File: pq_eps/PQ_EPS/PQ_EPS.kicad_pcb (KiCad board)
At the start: 2 copper layers, 40 x 40 mm, 77 parts, among them IC2 ISL9120IRTNZ, J1 SLW-110-01-X-S, J2 SLW-110-01-X-S, J3 SLW-110-01-X-S, J4 SLW-110-01-X-S, Q1 SIR424DP-T1-GE3

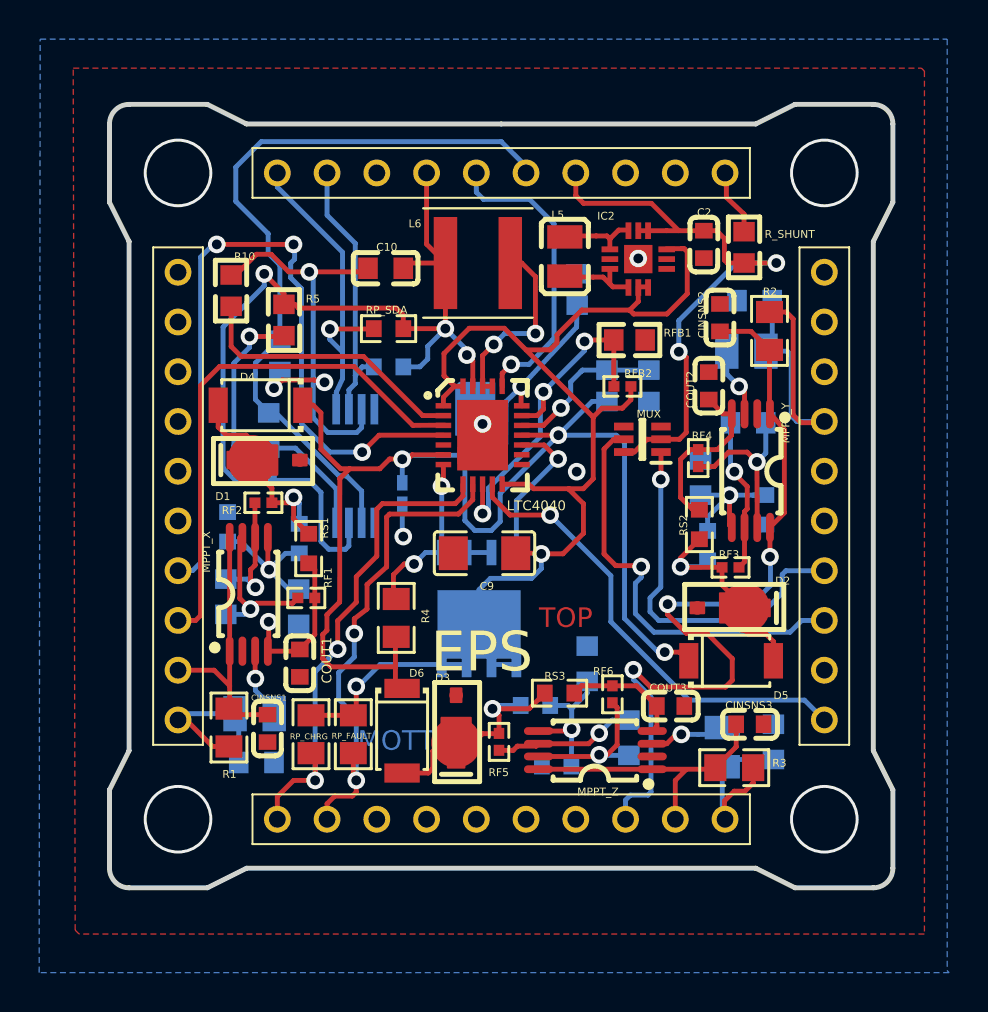
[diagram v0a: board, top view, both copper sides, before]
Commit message: eps port to kicad corrected
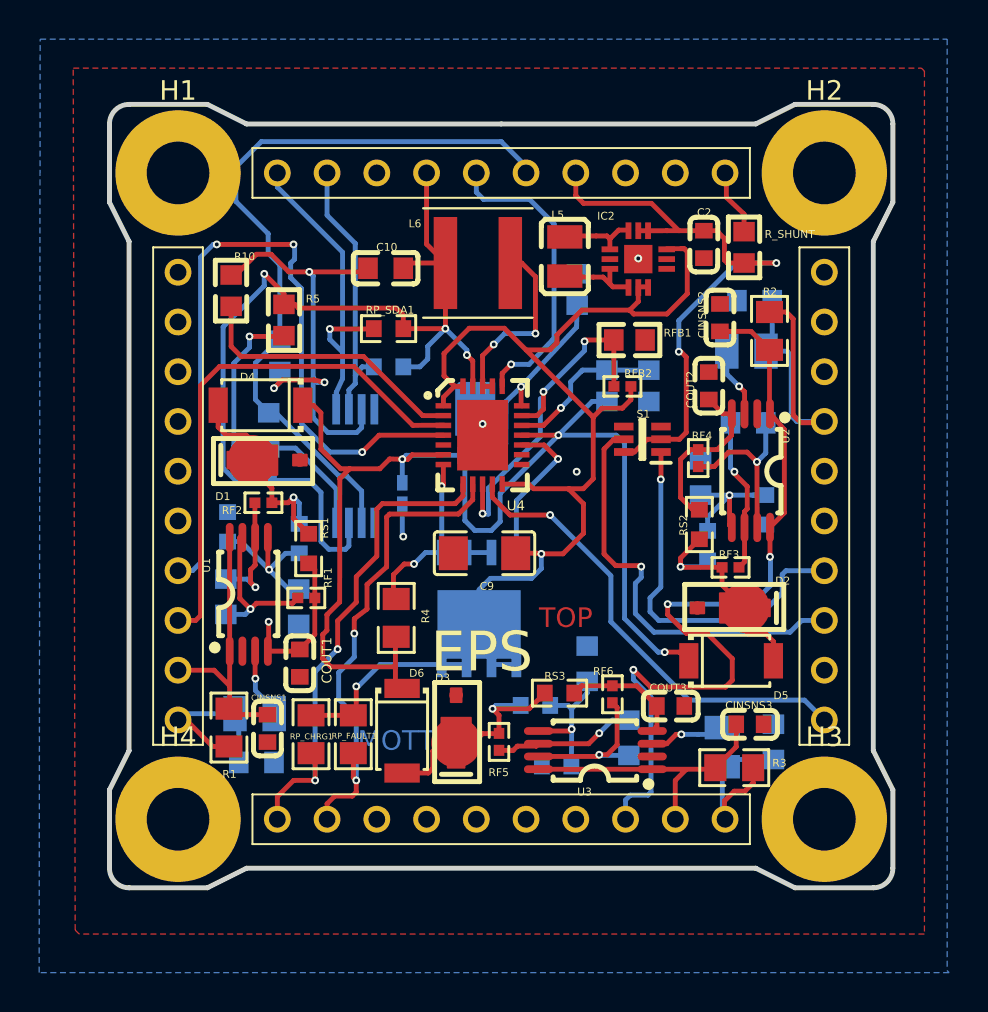
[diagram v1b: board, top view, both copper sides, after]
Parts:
- added H1: MountingHole_Pad, MountingHole:MountingHole_3.2mm_M3_Pad, F.Cu at (85.2, 41.5)
- added H2: MountingHole_Pad, MountingHole:MountingHole_3.2mm_M3_Pad, F.Cu at (118.2, 41.5)
- added H3: MountingHole_Pad, MountingHole:MountingHole_3.2mm_M3_Pad, F.Cu at (118.2, 74.5)
- added H4: MountingHole_Pad, MountingHole:MountingHole_3.2mm_M3_Pad, F.Cu at (85.2, 74.5)
- CINSNS1, CINSNS2, CINSNS3: value 10u -> 1n
- D4, D5, D6: value PDZVTR4.7B -> shottky
- J1, J2, J3, J4: value SLW-110-01-X-S -> SLW-110-01-T-S
- RFB1: value 100m -> 68k
- renumbered DS2782E+ to IC1, RP_CHRG to RP_CHRG1, RP_FAULT to RP_FAULT1, RP_SCL to RP_SCL1, RP_SDA to RP_SDA1, MUX to S1, MPPT_X to U1, MPPT_Y to U2, MPPT_Z to U3, LTC4040 to U4
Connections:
- C1 pad 1: (no net) -> Net-(C1-Pad1)
- C1 pad 2: (no net) -> /BATT-
- C10 pad 1: (no net) -> /BATT+
- C10 pad 2: (no net) -> GND
- C2 pad 1: (no net) -> GND
- C2 pad 2: (no net) -> /VCC
- C8 pad 1: (no net) -> /OVSNS
- C8 pad 2: (no net) -> GND
- C9 pad 1: (no net) -> /CHOUT
- C9 pad 2: (no net) -> GND
- CF1 pad 1: (no net) -> Net-(CF1-Pad1)
- CF1 pad 2: (no net) -> Net-(CF1-Pad2)
- CF2 pad 1: (no net) -> Net-(CF2-Pad1)
- CF2 pad 2: (no net) -> Net-(CF2-Pad2)
- CF3 pad 1: (no net) -> Net-(CF3-Pad1)
- CF3 pad 2: (no net) -> Net-(CF3-Pad2)
- CIN1 pad 1: (no net) -> GND
- CIN1 pad 2: (no net) -> /SOLAR_X
- CIN2 pad 1: (no net) -> GND
- CIN2 pad 2: (no net) -> /SOLAR_Y
- CIN3 pad 1: (no net) -> GND
- CIN3 pad 2: (no net) -> /SOLAR_Z
- CINSNS1 pad 1: (no net) -> GND
- CINSNS1 pad 2: (no net) -> /MPPT_X
- CINSNS2 pad 1: (no net) -> GND
- CINSNS2 pad 2: (no net) -> /MPPT_Y
- CINSNS3 pad 1: (no net) -> GND
- CINSNS3 pad 2: (no net) -> /MPPT_Z
- COUT1 pad 1: (no net) -> GND
- COUT1 pad 2: (no net) -> Net-(COUT1-Pad2)
- COUT2 pad 1: (no net) -> GND
- COUT2 pad 2: (no net) -> Net-(COUT2-Pad2)
- COUT3 pad 1: (no net) -> GND
- COUT3 pad 2: (no net) -> Net-(COUT3-Pad2)
- COUTSNS1 pad 1: (no net) -> GND
- COUTSNS1 pad 2: (no net) -> Net-(COUTSNS1-Pad2)
- COUTSNS2 pad 1: (no net) -> GND
- COUTSNS2 pad 2: (no net) -> Net-(COUTSNS2-Pad2)
- COUTSNS3 pad 1: (no net) -> GND
- COUTSNS3 pad 2: (no net) -> Net-(COUTSNS3-Pad2)
- D1 pad 1: (no net) -> GND
- D1 pad 2: (no net) -> Net-(D1-Pad2)
- D2 pad 1: (no net) -> GND
- D2 pad 2: (no net) -> Net-(D2-Pad2)
- D3 pad 1: (no net) -> GND
- D3 pad 2: (no net) -> Net-(D3-Pad2)
- D4 pad 1: (no net) -> /OVSNS
- D4 pad 2: (no net) -> Net-(D1-Pad2)
- D5 pad 1: (no net) -> /OVSNS
- D5 pad 2: (no net) -> Net-(D2-Pad2)
- D6 pad 1: (no net) -> /OVSNS
- D6 pad 2: (no net) -> Net-(D3-Pad2)
- IC1 pad 1: (no net) -> unconnected-(IC1-Pad1)
- IC1 pad 2: (no net) -> /BATT-
- IC1 pad 3: (no net) -> Net-(IC1-Pad3)
- IC1 pad 4: (no net) -> Net-(C1-Pad1)
- IC1 pad 5: (no net) -> /SCL
- IC1 pad 6: (no net) -> /SCL
- IC1 pad 7: (no net) -> GND
- IC1 pad 8: (no net) -> unconnected-(IC1-Pad8)
- IC2 pad 1: (no net) -> Net-(L5-Pad2)
- IC2 pad 10: (no net) -> /VCC
- IC2 pad 11: (no net) -> /VCC
- IC2 pad 12: (no net) -> Net-(L5-Pad2)
- IC2 pad 13: (no net) -> GND
- IC2 pad 2: (no net) -> GND
- IC2 pad 3: (no net) -> Net-(L5-Pad1)
- IC2 pad 4: (no net) -> Net-(L5-Pad1)
- IC2 pad 5: (no net) -> /CHOUT
- IC2 pad 6: (no net) -> /CHOUT
- IC2 pad 7: (no net) -> GND
- IC2 pad 8: (no net) -> GND
- IC2 pad 9: (no net) -> /CHOUT
- J1 pad 1: (no net) -> /SCL
- J1 pad 10: (no net) -> /VCC
- J1 pad 2: (no net) -> /SCL
- J1 pad 3: (no net) -> unconnected-(J1-Pad3)
- J1 pad 4: (no net) -> /BATT+
- J1 pad 5: (no net) -> /PFO
- J1 pad 6: (no net) -> /BATT-
- J1 pad 7: (no net) -> unconnected-(J1-Pad7)
- J1 pad 8: (no net) -> unconnected-(J1-Pad8)
- J1 pad 9: (no net) -> GND
- J2 pad 1: (no net) -> unconnected-(J2-Pad1)
- J2 pad 10: (no net) -> /RST
- J2 pad 2: (no net) -> unconnected-(J2-Pad2)
- J2 pad 3: (no net) -> unconnected-(J2-Pad3)
- J2 pad 4: (no net) -> /SOLAR_Y
- J2 pad 5: (no net) -> unconnected-(J2-Pad5)
- J2 pad 6: (no net) -> unconnected-(J2-Pad6)
- J2 pad 7: (no net) -> /SEL
- J2 pad 8: (no net) -> /HEATER
- J2 pad 9: (no net) -> unconnected-(J2-Pad9)
- J3 pad 1: (no net) -> /CHRG
- J3 pad 10: (no net) -> /SOLAR_Z
- J3 pad 2: (no net) -> /FAULT
- J3 pad 3: (no net) -> unconnected-(J3-Pad3)
- J3 pad 4: (no net) -> unconnected-(J3-Pad4)
- J3 pad 5: (no net) -> unconnected-(J3-Pad5)
- J3 pad 6: (no net) -> unconnected-(J3-Pad6)
- J3 pad 7: (no net) -> unconnected-(J3-Pad7)
- J3 pad 8: (no net) -> /MPPT_Y
- J3 pad 9: (no net) -> /MPPT_Z
- J4 pad 1: (no net) -> unconnected-(J4-Pad1)
- J4 pad 10: (no net) -> /SOLAR_X
- J4 pad 2: (no net) -> unconnected-(J4-Pad2)
- J4 pad 3: (no net) -> unconnected-(J4-Pad3)
- J4 pad 4: (no net) -> unconnected-(J4-Pad4)
- J4 pad 5: (no net) -> unconnected-(J4-Pad5)
- J4 pad 6: (no net) -> unconnected-(J4-Pad6)
- J4 pad 7: (no net) -> /CHGOFF
- J4 pad 8: (no net) -> /CLPROG
- J4 pad 9: (no net) -> /MPPT_X
- L1 pad 1: (no net) -> /SOLAR_X
- L1 pad 2: (no net) -> Net-(U1-Pad3)
- L2 pad 1: (no net) -> /SOLAR_Y
- L2 pad 2: (no net) -> Net-(L2-Pad2)
- L3 pad 1: (no net) -> /SOLAR_Z
- L3 pad 2: (no net) -> Net-(U3-Pad3)
- L5 pad 1: (no net) -> Net-(L5-Pad1)
- L5 pad 2: (no net) -> Net-(L5-Pad2)
- L6 pad 1: (no net) -> /BATT+
- L6 pad 2: (no net) -> Net-(U4-Pad21)
- Q1 pad 1: (no net) -> Net-(Q1-Pad1)
- Q1 pad 2: (no net) -> Net-(Q1-Pad1)
- Q1 pad 3: (no net) -> Net-(Q1-Pad1)
- Q1 pad 4: (no net) -> Net-(Q1-Pad4)
- Q1 pad 5: (no net) -> /CHOUT
- Q1 pad 6: (no net) -> /CHOUT
- Q1 pad 7: (no net) -> /CHOUT
- Q1 pad 8: (no net) -> /CHOUT
- R1 pad 1: (no net) -> /SOLAR_X
- R1 pad 2: (no net) -> /MPPT_X
- R10 pad 1: (no net) -> /PROG
- R10 pad 2: (no net) -> GND
- R2 pad 1: (no net) -> /SOLAR_Y
- R2 pad 2: (no net) -> /MPPT_Y
- R3 pad 1: (no net) -> /SOLAR_Z
- R3 pad 2: (no net) -> /MPPT_Z
- R4 pad 1: (no net) -> Net-(Q1-Pad1)
- R4 pad 2: (no net) -> /OVSNS
- R5 pad 1: (no net) -> /BATT+
- R5 pad 2: (no net) -> Net-(C1-Pad1)
- R6 pad 1: (no net) -> GND
- R6 pad 2: (no net) -> /BATT-
- R7 pad 1: (no net) -> /BATT+
- R7 pad 2: (no net) -> Net-(IC1-Pad3)
- R8 pad 1: (no net) -> GND
- R8 pad 2: (no net) -> /NTC
- R9 pad 1: (no net) -> /NTC
- R9 pad 2: (no net) -> /OVSNS
- RF1 pad 1: (no net) -> Net-(CF1-Pad2)
- RF1 pad 2: (no net) -> Net-(COUT1-Pad2)
- RF2 pad 1: (no net) -> Net-(CF1-Pad1)
- RF2 pad 2: (no net) -> Net-(D1-Pad2)
- RF3 pad 1: (no net) -> Net-(CF2-Pad1)
- RF3 pad 2: (no net) -> Net-(D2-Pad2)
- RF4 pad 1: (no net) -> Net-(CF2-Pad2)
- RF4 pad 2: (no net) -> Net-(COUT2-Pad2)
- RF5 pad 1: (no net) -> Net-(CF3-Pad1)
- RF5 pad 2: (no net) -> Net-(D3-Pad2)
- RF6 pad 1: (no net) -> Net-(CF3-Pad2)
- RF6 pad 2: (no net) -> Net-(COUT3-Pad2)
- RFB1 pad 1: (no net) -> Net-(RFB1-Pad1)
- RFB1 pad 2: (no net) -> GND
- RFB2 pad 1: (no net) -> Net-(RFB1-Pad1)
- RFB2 pad 2: (no net) -> /CHOUT
- RH1 pad 1: (no net) -> Net-(COUTSNS1-Pad2)
- RH1 pad 2: (no net) -> Net-(D1-Pad2)
- RH2 pad 1: (no net) -> Net-(COUTSNS2-Pad2)
- RH2 pad 2: (no net) -> Net-(D2-Pad2)
- RH3 pad 1: (no net) -> Net-(COUTSNS3-Pad2)
- RH3 pad 2: (no net) -> Net-(D3-Pad2)
- RL1 pad 1: (no net) -> GND
- RL1 pad 2: (no net) -> Net-(COUTSNS1-Pad2)
- RL2 pad 1: (no net) -> GND
- RL2 pad 2: (no net) -> Net-(COUTSNS2-Pad2)
- RL3 pad 1: (no net) -> GND
- RL3 pad 2: (no net) -> Net-(COUTSNS3-Pad2)
- RPF1 pad 1: (no net) -> /OVSNS
- RPF1 pad 2: (no net) -> Net-(RPF1-Pad2)
- RPF2 pad 1: (no net) -> Net-(RPF1-Pad2)
- RPF2 pad 2: (no net) -> GND
- RP_CHRG1 pad 1: (no net) -> /CHRG
- RP_CHRG1 pad 2: (no net) -> /CHOUT
- RP_FAULT1 pad 1: (no net) -> /FAULT
- RP_FAULT1 pad 2: (no net) -> /CHOUT
- RP_SCL1 pad 1: (no net) -> /BATT+
- RP_SCL1 pad 2: (no net) -> /SCL
- RP_SDA1 pad 1: (no net) -> /BATT+
- RP_SDA1 pad 2: (no net) -> /SCL
- RS1 pad 1: (no net) -> Net-(COUT1-Pad2)
- RS1 pad 2: (no net) -> Net-(D1-Pad2)
- RS2 pad 1: (no net) -> Net-(COUT2-Pad2)
- RS2 pad 2: (no net) -> Net-(D2-Pad2)
- RS3 pad 1: (no net) -> Net-(COUT3-Pad2)
- RS3 pad 2: (no net) -> Net-(D3-Pad2)
- S1 pad 1: (no net) -> /SEL
- S1 pad 2: (no net) -> /TOTAL_CURRENT
- S1 pad 3: (no net) -> GND
- S1 pad 4: (no net) -> GND
- S1 pad 5: (no net) -> /HEATER
- S1 pad 6: (no net) -> /TOTAL_CURRENT
- U1 pad 1: (no net) -> /MPPT_X
- U1 pad 2: (no net) -> GND
- U1 pad 3: (no net) -> Net-(U1-Pad3)
- U1 pad 4: (no net) -> Net-(COUT1-Pad2)
- U1 pad 5: (no net) -> Net-(COUTSNS1-Pad2)
- U1 pad 6: (no net) -> Net-(CF1-Pad1)
- U1 pad 7: (no net) -> Net-(CF1-Pad2)
- U1 pad 8: (no net) -> /MPPT_X
- U2 pad 1: (no net) -> /MPPT_Y
- U2 pad 2: (no net) -> GND
- U2 pad 3: (no net) -> Net-(L2-Pad2)
- U2 pad 4: (no net) -> Net-(COUT2-Pad2)
- U2 pad 5: (no net) -> Net-(COUTSNS2-Pad2)
- U2 pad 6: (no net) -> Net-(CF2-Pad1)
- U2 pad 7: (no net) -> Net-(CF2-Pad2)
- U2 pad 8: (no net) -> /MPPT_Y
- U3 pad 1: (no net) -> /MPPT_Z
- U3 pad 2: (no net) -> GND
- U3 pad 3: (no net) -> Net-(U3-Pad3)
- U3 pad 4: (no net) -> Net-(COUT3-Pad2)
- U3 pad 5: (no net) -> Net-(COUTSNS3-Pad2)
- U3 pad 6: (no net) -> Net-(CF3-Pad1)
- U3 pad 7: (no net) -> Net-(CF3-Pad2)
- U3 pad 8: (no net) -> /MPPT_Z
- U4 pad 1: (no net) -> /CHOUT
- U4 pad 10: (no net) -> Net-(RFB1-Pad1)
- U4 pad 11: (no net) -> /RST
- U4 pad 12: (no net) -> /CHOUT
- U4 pad 13: (no net) -> GND
- U4 pad 14: (no net) -> GND
- U4 pad 15: (no net) -> Net-(Q1-Pad4)
- U4 pad 16: (no net) -> /OVSNS
- U4 pad 17: (no net) -> /NTC
- U4 pad 18: (no net) -> Net-(RFB1-Pad1)
- U4 pad 19: (no net) -> Net-(RPF1-Pad2)
- U4 pad 2: (no net) -> /PROG
- U4 pad 20: (no net) -> /PFO
- U4 pad 21: (no net) -> Net-(U4-Pad21)
- U4 pad 22: (no net) -> Net-(U4-Pad21)
- U4 pad 23: (no net) -> /BATT+
- U4 pad 24: (no net) -> /CHOUT
- U4 pad 25: (no net) -> GND
- U4 pad 3: (no net) -> /CLPROG
- U4 pad 4: (no net) -> /CHGOFF
- U4 pad 5: (no net) -> GND
- U4 pad 6: (no net) -> /OVSNS
- U4 pad 7: (no net) -> Net-(Q1-Pad1)
- U4 pad 8: (no net) -> /CHRG
- U4 pad 9: (no net) -> /FAULT
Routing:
- net (no net): track 854.4 -> 0.00 mm, vias 63 -> 0
- net /OVSNS: track 0.00 -> 64.3 mm, vias 0 -> 3
- net /CHOUT: track 0.00 -> 63.8 mm, vias 0 -> 2
- net /MPPT_Y: track 0.00 -> 41.7 mm, vias 0 -> 3
- net /BATT+: track 0.00 -> 41.4 mm, vias 0 -> 3
- net /CHGOFF: track 0.00 -> 39.6 mm, vias 0 -> 3
- net /BATT-: track 0.00 -> 38.6 mm
- net /VCC: track 0.00 -> 34.7 mm, vias 0 -> 2
- net /SCL: track 0.00 -> 31.2 mm, vias 0 -> 1
- net /CLPROG: track 0.00 -> 27.1 mm
- net /CHRG: track 0.00 -> 25.3 mm, vias 0 -> 2
- net GND: track 0.00 -> 25.3 mm, vias 0 -> 7
- net /FAULT: track 0.00 -> 25.1 mm, vias 0 -> 2
- net /RST: track 0.00 -> 23.7 mm, vias 0 -> 1
- net /HEATER: track 0.00 -> 21.5 mm, vias 0 -> 1
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- added copper zone on B.Cu, net GND
- added copper zone on F.Cu, net GND
- removed copper zone on B.Cu, net (none)
- removed copper zone on F.Cu, net (none)

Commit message: EPS LTC 4040 correction and layout revamp
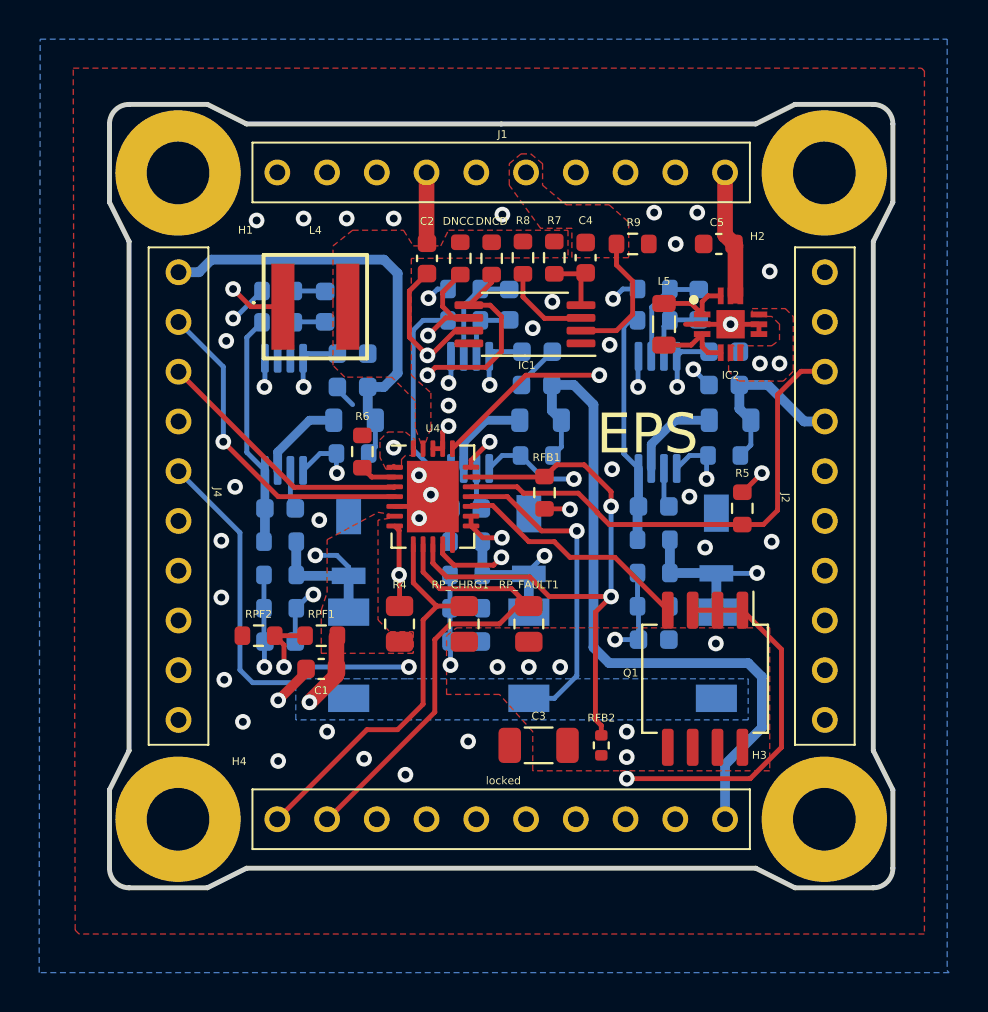
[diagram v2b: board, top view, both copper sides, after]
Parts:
- removed C10: 10u, easyeda:C0603
- removed C8: 2.2u, easyeda:C0402
- removed C9: 100u, easyeda:C1206
- removed L6: 2.2u, easyeda:L_COILCRAFT_XAL5030
- removed R10: 14k, easyeda:R0603
- removed RP_SCL1, RP_SDA1: 20k, easyeda:R0603
- removed R_SHUNT: 100m, easyeda:R0603
- removed S1: MUX, easyeda:SOT65P210X110-6N
- added C3: 100u, Capacitor_SMD:C_1206_3216Metric, F.Cu at (103.6, 70.7)
- added C4: 0.1u, Capacitor_SMD:C_0603_1608Metric, F.Cu at (106.0, 45.8)
- added C5: 22u, Capacitor_SMD:C_0603_1608Metric, F.Cu at (112.8, 45.1)
- added DNCC: 20k, Resistor_SMD:R_0603_1608Metric, F.Cu at (99.6, 45.8)
- added DNCD: 20k, Resistor_SMD:R_0603_1608Metric, F.Cu at (101.2, 45.8)
- added L4: XAL5030-222MEC, SamacSys_Parts:XAL5030222MEC, F.Cu at (92.2, 48.3)
- C1: value 0.1u -> 2.2u; footprint easyeda:C0603 -> Capacitor_SMD:C_0603_1608Metric
- C2: value 22u -> 10u; footprint easyeda:C0603 -> Capacitor_SMD:C_0603_1608Metric
- CF1, CF2, CF3, CIN1, CIN2, CIN3, CINSNS1, CINSNS2, CINSNS3, COUT1, COUT2, COUT3, COUTSNS1, COUTSNS2, COUTSNS3: footprint easyeda:C0603 -> Capacitor_SMD:C_0603_1608Metric; moved to B.Cu
- D1, D2, D3: footprint easyeda:DIO_SMM4F5.0A-TR -> SamacSys_Parts:SMM4F15ATR; moved to B.Cu
- D4, D5, D6: footprint easyeda:SOD-128_L3.7-W2.5-LS4.7-FD -> Diode_SMD:D_SOD-128; moved to B.Cu
- IC1: footprint easyeda:SOP65P640X110-8N -> Package_SO:TSSOP-8_4.4x3mm_P0.65mm
- IC2: footprint easyeda:QFN50P300X300X75-13N -> SamacSys_Parts:QFN50P300X300X75-13N-D
- J1, J2, J4: footprint easyeda:SLW-110-01-X-S -> NSL_Connectors:SLW-110-01-X-S
- L1, L2, L3: footprint easyeda:L0806 -> Inductor_SMD:L_0805_2012Metric; moved to B.Cu
- L5: footprint easyeda:L0806 -> Inductor_SMD:L_0805_2012Metric
- Q1: footprint easyeda:POWERPAK-SO-8_L6.2-W5.2-P1.27-BL-EP -> Package_SO:SO-8_5.3x6.2mm_P1.27mm
- R1, R2, R3: footprint easyeda:R0805 -> Resistor_SMD:R_0603_1608Metric; moved to B.Cu
- R4, RP_CHRG1, RP_FAULT1: footprint easyeda:R0805 -> Resistor_SMD:R_0805_2012Metric
- R5: value 510 -> 10k; footprint easyeda:R0603 -> Resistor_SMD:R_0603_1608Metric
- R6: value 15m -> 2k; footprint easyeda:R0603 -> Resistor_SMD:R_0603_1608Metric
- R7: value 1k -> 510; footprint easyeda:R0402 -> Resistor_SMD:R_0603_1608Metric
- R8: value 10k -> 1k; footprint easyeda:R0603 -> Resistor_SMD:R_0603_1608Metric
- R9: value 10k -> 15m; footprint easyeda:R0603 -> Resistor_SMD:R_0603_1608Metric
- RF1, RF2, RF3, RF4, RF5, RF6: footprint easyeda:R0402 -> Resistor_SMD:R_0603_1608Metric; moved to B.Cu
- RFB1, RPF1, RPF2: footprint easyeda:R0603 -> Resistor_SMD:R_0603_1608Metric
- RFB2: footprint easyeda:R0402 -> Resistor_SMD:R_0402_1005Metric
- RH1, RH2, RH3, RL1, RL2, RL3, RS1, RS2, RS3: footprint easyeda:R0603 -> Resistor_SMD:R_0603_1608Metric; moved to B.Cu
- U1, U2, U3: footprint easyeda:TSSOP-8_L4.4-W3.0-P0.65-LS6.4-BL -> Package_SO:TSSOP-8_4.4x3mm_P0.65mm; moved to B.Cu
- U4: footprint easyeda:VQFN-24_L5.0-W4.0-P0.50-BL-EP -> Package_DFN_QFN:QFN-24-1EP_4x5mm_P0.5mm_EP2.65x3.65mm
- locked: renamed from J3; footprint easyeda:SLW-110-01-X-S -> NSL_Connectors:SLW-110-01-X-S
- moved R5 25.3 mm to (114.0, 58.6), turned to 90 degrees
- moved RPF2 24.0 mm to (89.3, 65.1), turned to 180 degrees
- moved RF5 23.2 mm to (99.8, 47.4), turned to 180 degrees
- moved CF3 22.9 mm to (102.1, 48.2)
- moved CINSNS3 21.9 mm to (103.5, 50.6)
- moved CIN3 21.9 mm to (103.5, 52.3), turned to 0 degrees
- moved RF6 20.5 mm to (99.8, 49.0), turned to 180 degrees
- moved CIN1 19.8 mm to (94.1, 52.4)
- moved CINSNS1 19.6 mm to (94.1, 50.7), turned to 180 degrees
- moved L3 19.1 mm to (103.7, 54.1), turned to 180 degrees
- moved R3 18.9 mm to (103.5, 55.9)
- moved R7 18.7 mm to (104.4, 45.8), turned to -90 degrees
- moved U3 18.4 mm to (100.1, 53.7)
- moved RFB2 18.4 mm to (106.8, 70.7), turned to -90 degrees
- moved L1 15.8 mm to (94.2, 54.1), turned to 0 degrees
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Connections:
- C1 pad 1: Net-(C1-Pad1) -> /OVSNS
- C1 pad 2: /BATT- -> GND
- C2 pad 1: GND -> /KILLSWITCH+
- C2 pad 2: /VCC -> GND
- CINSNS1 pad 2: /MPPT_X -> Net-(CINSNS1-Pad2)
- CINSNS2 pad 2: /MPPT_Y -> Net-(CINSNS2-Pad2)
- CINSNS3 pad 2: /MPPT_Z -> Net-(CINSNS3-Pad2)
- IC1 pad 4: Net-(C1-Pad1) -> Net-(C4-Pad1)
- IC1 pad 5: /SCL -> /SDA
- J1 pad 1: /SCL -> /SDA
- J1 pad 4: /BATT+ -> /KILLSWITCH+
- J2 pad 10: /RST -> GND
- J2 pad 3: unconnected-(J2-Pad3) -> /BATT_NTC
- J2 pad 7: /SEL -> GND
- J2 pad 8: /HEATER -> unconnected-(J2-Pad8)
- J4 pad 1: unconnected-(J4-Pad1) -> /SOLAR_X
- J4 pad 10: /SOLAR_X -> unconnected-(J4-Pad10)
- J4 pad 2: unconnected-(J4-Pad2) -> /CHGOFF
- J4 pad 3: unconnected-(J4-Pad3) -> /CLPROG
- J4 pad 5: unconnected-(J4-Pad5) -> /RST
- J4 pad 7: /CHGOFF -> unconnected-(J4-Pad7)
- J4 pad 8: /CLPROG -> unconnected-(J4-Pad8)
- J4 pad 9: /MPPT_X -> unconnected-(J4-Pad9)
- L1 pad 1: /SOLAR_X -> Net-(L1-Pad1)
- L1 pad 2: Net-(U1-Pad3) -> /SOLAR_X
- R1 pad 2: /MPPT_X -> Net-(CINSNS1-Pad2)
- R2 pad 2: /MPPT_Y -> Net-(CINSNS2-Pad2)
- R3 pad 2: /MPPT_Z -> Net-(CINSNS3-Pad2)
- R5 pad 1: /BATT+ -> /BATT_NTC
- R5 pad 2: Net-(C1-Pad1) -> /VCC
- R6 pad 1: GND -> /PROG
- R6 pad 2: /BATT- -> GND
- R7 pad 1: /BATT+ -> /KILLSWITCH+
- R7 pad 2: Net-(IC1-Pad3) -> Net-(C4-Pad1)
- R8 pad 1: GND -> /KILLSWITCH+
- R8 pad 2: /NTC -> Net-(IC1-Pad3)
- R9 pad 1: /NTC -> GND
- R9 pad 2: /OVSNS -> /BATT-
- U1 pad 1: /MPPT_X -> Net-(CINSNS1-Pad2)
- U1 pad 3: Net-(U1-Pad3) -> Net-(L1-Pad1)
- U1 pad 8: /MPPT_X -> Net-(CINSNS1-Pad2)
- U2 pad 1: /MPPT_Y -> Net-(CINSNS2-Pad2)
- U2 pad 8: /MPPT_Y -> Net-(CINSNS2-Pad2)
- U3 pad 1: /MPPT_Z -> Net-(CINSNS3-Pad2)
- U3 pad 8: /MPPT_Z -> Net-(CINSNS3-Pad2)
- U4 pad 12: /CHOUT -> GND
- U4 pad 13: GND -> /CHOUT
- U4 pad 14: GND -> /CHOUT
- U4 pad 17: /NTC -> /BATT_NTC
- U4 pad 23: /BATT+ -> /KILLSWITCH+
- locked pad 8: /MPPT_Y -> unconnected-(J3-Pad8)
- locked pad 9: /MPPT_Z -> unconnected-(J3-Pad9)
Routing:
- net /CHOUT: track 63.8 -> 2.46 mm, vias 2 -> 8
- net /OVSNS: track 64.3 -> 20.4 mm, vias 3 -> 2
- net /MPPT_Y: track 41.7 -> 0.00 mm, vias 3 -> 0
- net /BATT+: track 41.4 -> 0.00 mm, vias 3 -> 0
- net Net-(Q1-Pad1): track 11.1 -> 45.8 mm
- net /BATT-: track 38.6 -> 6.92 mm
- net /SOLAR_Z: track 9.08 -> 36.2 mm
- net /BATT_NTC: track 0.00 -> 25.6 mm
- net /SDA: track 0.00 -> 23.6 mm, vias 0 -> 1
- net /CHGOFF: track 39.6 -> 17.0 mm, vias 3 -> 1
- net /HEATER: track 21.5 -> 0.00 mm, vias 1 -> 0
- net /SEL: track 19.1 -> 0.00 mm, vias 1 -> 0
- net Net-(D2-Pad2): track 11.9 -> 28.3 mm, vias 1 -> 2
- net Net-(COUTSNS3-Pad2): track 7.54 -> 23.6 mm, vias 1 -> 2
- net Net-(C1-Pad1): track 15.6 -> 0.00 mm, vias 1 -> 0
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- added copper zone on F.Cu, net /BATT-
- added copper zone on F.Cu, net /CHOUT
- added copper zone on In2.Cu, net /CHOUT
- added copper zone on F.Cu, net /KILLSWITCH+
- added copper zone on B.Cu, net /OVSNS
- added copper zone on F.Cu, net /OVSNS
- added copper zone on In1.Cu, net GND
- added copper zone on In2.Cu, net GND
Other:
- copper layers 2 -> 4
- board text removed: "BOTTOM"
- board text removed: "TOP"

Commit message: EPS board revised and Guillem approved
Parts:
- added G***: LOGO, LOGO, F.Cu at (89.8, 59.8)
- added G***: LOGO, LOGO, F.Cu at (89.8, 61.2)
- Q1: footprint Package_SO:SO-8_5.3x6.2mm_P1.27mm -> Package_SO:PowerPAK_SO-8_Single
- moved RFB2 6.31 mm to (105.6, 64.5)
- moved R4 1.82 mm to (95.4, 63.1), turned to 180 degrees
- moved Q1 0.85 mm to (112.1, 66.4)
- renumbered DNCC to DNC1, DNCD to DNC2
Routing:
- net Net-(RFB1-Pad1): track 31.6 -> 24.8 mm
- net /KILLSWITCH+: track 3.62 -> 10.2 mm, vias 0 -> 3
- net /RST: track 32.4 -> 38.7 mm, vias 2 -> 1
- net Net-(L4-Pad1): track 18.6 -> 13.3 mm, vias 2 -> 0
- net Net-(Q1-Pad1): track 45.8 -> 43.0 mm
- net GND: track 34.2 -> 36.6 mm, vias 40 -> 46
- net /OVSNS: track 20.4 -> 18.2 mm, vias 2 -> 5
- net Net-(COUT3-Pad2): track 14.2 -> 12.9 mm
- net /SCL: track 16.5 -> 15.4 mm, vias 1 -> 0
- net Net-(RPF1-Pad2): track 24.8 -> 25.5 mm
- net /PFO: track 22.0 -> 22.6 mm
- net /SDA: track 23.6 -> 23.0 mm, vias 1 -> 0
- added copper zone on In2.Cu, net /KILLSWITCH+
- removed copper zone on In2.Cu, net GND
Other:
- board text added: "NanoSat Lab"
- board text added: "PoCat EPS"
- board text removed: "EPS"

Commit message: Functional revision and finishing touches part I
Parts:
- removed G*** (x2): LOGO, LOGO
- added Annotation1: Silkscreen_Annotation, symbols-nsl:Bridgemaker, F.Cu at (89.8, 59.7)
- added Annotation2: Silkscreen_Annotation, symbols-nsl:NakNak, F.Cu at (89.9, 62.2)
- D1, D2, D3: value SMM4F5.0A -> SMM4F; footprint SamacSys_Parts:SMM4F15ATR -> passive-nsl:SMM4F15ATR
- IC2: footprint SamacSys_Parts:QFN50P300X300X75-13N-D -> Package_DFN_QFN:QFN-12-1EP_3x3mm_P0.5mm_EP1.6x1.6mm
- J1, J2, J4, locked: footprint NSL_Connectors:SLW-110-01-X-S -> connector-nsl:SLW-110-01
- L4: footprint SamacSys_Parts:XAL5030222MEC -> passive-nsl:XAL5030222MEC
- moved D2 0.76 mm to (112.7, 60.6), turned to -90 degrees
- moved D3 0.75 mm to (103.3, 60.6), turned to -90 degrees
- moved D1 0.58 mm to (93.9, 60.5), turned to -90 degrees
- moved D6 0.18 mm to (103.3, 66.1)
- turned J1 to 90 degrees
- turned J2 to 0 degrees
- turned J4 to 0 degrees
- turned locked to 90 degrees
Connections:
- D1 pad 1: GND -> Net-(D1-Pad1)
- D1 pad 2: Net-(D1-Pad2) -> GND
- D2 pad 1: GND -> Net-(D2-Pad1)
- D2 pad 2: Net-(D2-Pad2) -> GND
- D3 pad 1: GND -> Net-(D3-Pad1)
- D3 pad 2: Net-(D3-Pad2) -> GND
- D4 pad 2: Net-(D1-Pad2) -> Net-(D1-Pad1)
- D5 pad 2: Net-(D2-Pad2) -> Net-(D2-Pad1)
- D6 pad 2: Net-(D3-Pad2) -> Net-(D3-Pad1)
- RF2 pad 2: Net-(D1-Pad2) -> Net-(D1-Pad1)
- RF3 pad 2: Net-(D2-Pad2) -> Net-(D2-Pad1)
- RF5 pad 2: Net-(D3-Pad2) -> Net-(D3-Pad1)
- RH1 pad 2: Net-(D1-Pad2) -> Net-(D1-Pad1)
- RH2 pad 2: Net-(D2-Pad2) -> Net-(D2-Pad1)
- RH3 pad 2: Net-(D3-Pad2) -> Net-(D3-Pad1)
- RS1 pad 2: Net-(D1-Pad2) -> Net-(D1-Pad1)
- RS2 pad 2: Net-(D2-Pad2) -> Net-(D2-Pad1)
- RS3 pad 2: Net-(D3-Pad2) -> Net-(D3-Pad1)
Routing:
- net Net-(D2-Pad1): track 0.00 -> 28.6 mm, vias 0 -> 2
- net Net-(D2-Pad2): track 28.3 -> 0.00 mm, vias 2 -> 0
- net Net-(D3-Pad1): track 0.00 -> 27.8 mm, vias 0 -> 2
- net Net-(D3-Pad2): track 27.0 -> 0.00 mm, vias 2 -> 0
- net Net-(D1-Pad2): track 25.3 -> 0.00 mm, vias 2 -> 0
- net Net-(D1-Pad1): track 0.00 -> 25.3 mm, vias 0 -> 2
- net GND: track 36.6 -> 39.3 mm
- net Net-(Q1-Pad1): track 43.0 -> 44.9 mm
- net /BATT_NTC: track 25.6 -> 26.3 mm
